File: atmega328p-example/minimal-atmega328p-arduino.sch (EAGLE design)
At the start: 39 parts, among them J1 3x2 M, J2 1x6 M, J3 629105136821, J4 POWER_JACK, Q1 PMV45EN2R, SW1 !RESET, U1 NCP1117ST50T3G, U4 ATMEGA328P-PU, X1 16 MHz

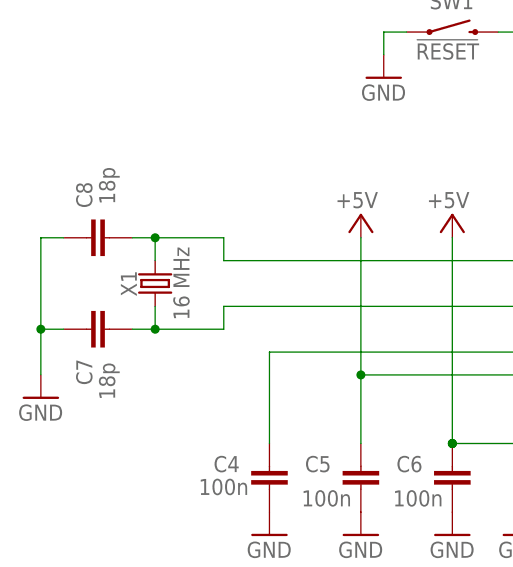
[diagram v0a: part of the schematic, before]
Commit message: Eeek! Bad cap values for the crystal oscillator. Changed from 18pF to 30 pF based on 18 pF load cap and 0805 capacitors.
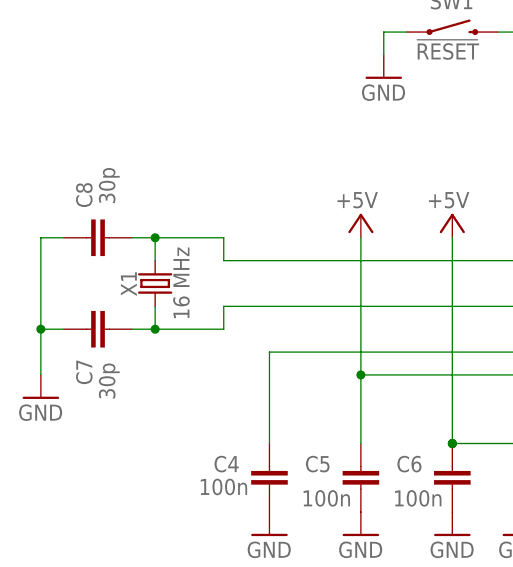
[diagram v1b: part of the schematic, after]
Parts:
- C7: value 18p -> 30p; DESC (none) -> CAP CER 30PF 50V C0G/NP0 0805
- C8: value 18p -> 30p; DESC (none) -> CAP CER 30PF 50V C0G/NP0 0805; MPN CL21C180JBANNNC -> CL21C300JBANNNC
- X1: DESC (none) -> CRYSTAL 16.000 MHZ 18PF SMD
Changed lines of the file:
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@@
 <part name="P+4" library="supply1" deviceset="+5V" device=""/>
 <part name="X1" library="SparkFun-Clocks" library_urn="urn:adsk.eagle:library:511" deviceset="CRYSTAL" device="SMD-HC49UP" package3d_urn="urn:adsk.eagle:package:37513/1" value="16 MHz">
+<attribute name="DESC" value="CRYSTAL 16.000 MHZ 18PF SMD"/>
 <attribute name="MFR" value="ECS"/>
 <attribute name="MPN" value="ECS-160-18-5PX-TR"/>
 </part>
-<part name="C7" library="rcl" library_urn="urn:adsk.eagle:library:334" deviceset="C-EU" device="C0805K" package3d_urn="urn:adsk.eagle:package:23681/2" value="18p">
+<part name="C7" library="rcl" library_urn="urn:adsk.eagle:library:334" deviceset="C-EU" device="C0805K" package3d_urn="urn:adsk.eagle:package:23681/2" value="30p">
 <spice>
 <pinmapping spiceprefix="C">
@@
 </pinmapping>
 </spice>
+<attribute name="DESC" value="CAP CER 30PF 50V C0G/NP0 0805"/>
 <attribute name="MFR" value="Samsung"/>
 <attribute name="MPN" value="CL21C180JBANNNC"/>
 </part>
-<part name="C8" library="rcl" library_urn="urn:adsk.eagle:library:334" deviceset="C-EU" device="C0805K" package3d_urn="urn:adsk.eagle:package:23681/2" value="18p">
+<part name="C8" library="rcl" library_urn="urn:adsk.eagle:library:334" deviceset="C-EU" device="C0805K" package3d_urn="urn:adsk.eagle:package:23681/2" value="30p">
 <spice>
 <pinmapping spiceprefix="C">
@@
 </pinmapping>
 </spice>
+<attribute name="DESC" value="CAP CER 30PF 50V C0G/NP0 0805"/>
 <attribute name="MFR" value="Samsung"/>
-<attribute name="MPN" value="CL21C180JBANNNC"/>
+<attribute name="MPN" value="CL21C300JBANNNC"/>
 </part>
 <part name="R2" library="rcl" library_urn="urn:adsk.eagle:library:334" deviceset="R-US_" device="R0805" package3d_urn="urn:adsk.eagle:package:23553/2" value="1K">
@@
 <attribute name="MFR" x="73.66" y="118.11" size="1.778" layer="96" rot="R90" display="off"/>
 <attribute name="MPN" x="73.66" y="118.11" size="1.778" layer="96" rot="R90" display="off"/>
+<attribute name="DESC" x="73.66" y="118.11" size="1.778" layer="96" rot="R90" display="off"/>
 </instance>
 <instance part="C7" gate="G$1" x="68.58" y="113.03" smashed="yes" rot="R270">
@@
 <attribute name="MFR" x="68.58" y="113.03" size="1.778" layer="96" rot="R270" display="off"/>
 <attribute name="MPN" x="68.58" y="113.03" size="1.778" layer="96" rot="R270" display="off"/>
+<attribute name="DESC" x="68.58" y="113.03" size="1.778" layer="96" rot="R270" display="off"/>
 </instance>
 <instance part="C8" gate="G$1" x="68.58" y="123.19" smashed="yes" rot="MR90">
@@
 <attribute name="MFR" x="68.58" y="123.19" size="1.778" layer="96" rot="MR90" display="off"/>
 <attribute name="MPN" x="68.58" y="123.19" size="1.778" layer="96" rot="MR90" display="off"/>
+<attribute name="DESC" x="68.58" y="123.19" size="1.778" layer="96" rot="MR90" display="off"/>
 </instance>
 <instance part="R2" gate="G$1" x="212.09" y="77.47" smashed="yes" rot="R180">
